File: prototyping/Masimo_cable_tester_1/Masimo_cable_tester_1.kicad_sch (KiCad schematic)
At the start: 27 parts, among them J1 Touchscreen HMI, J12 Barrel_Jack, J16 Debug Connections, J17 Banana Jack, J18 Massimo Connector, J2 Conn_01x28_Socket, J3 Conn_01x28_Socket, J4 SD Card Reader, K2 J104D2C5VDC.15S, U2 LM7805_TO220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

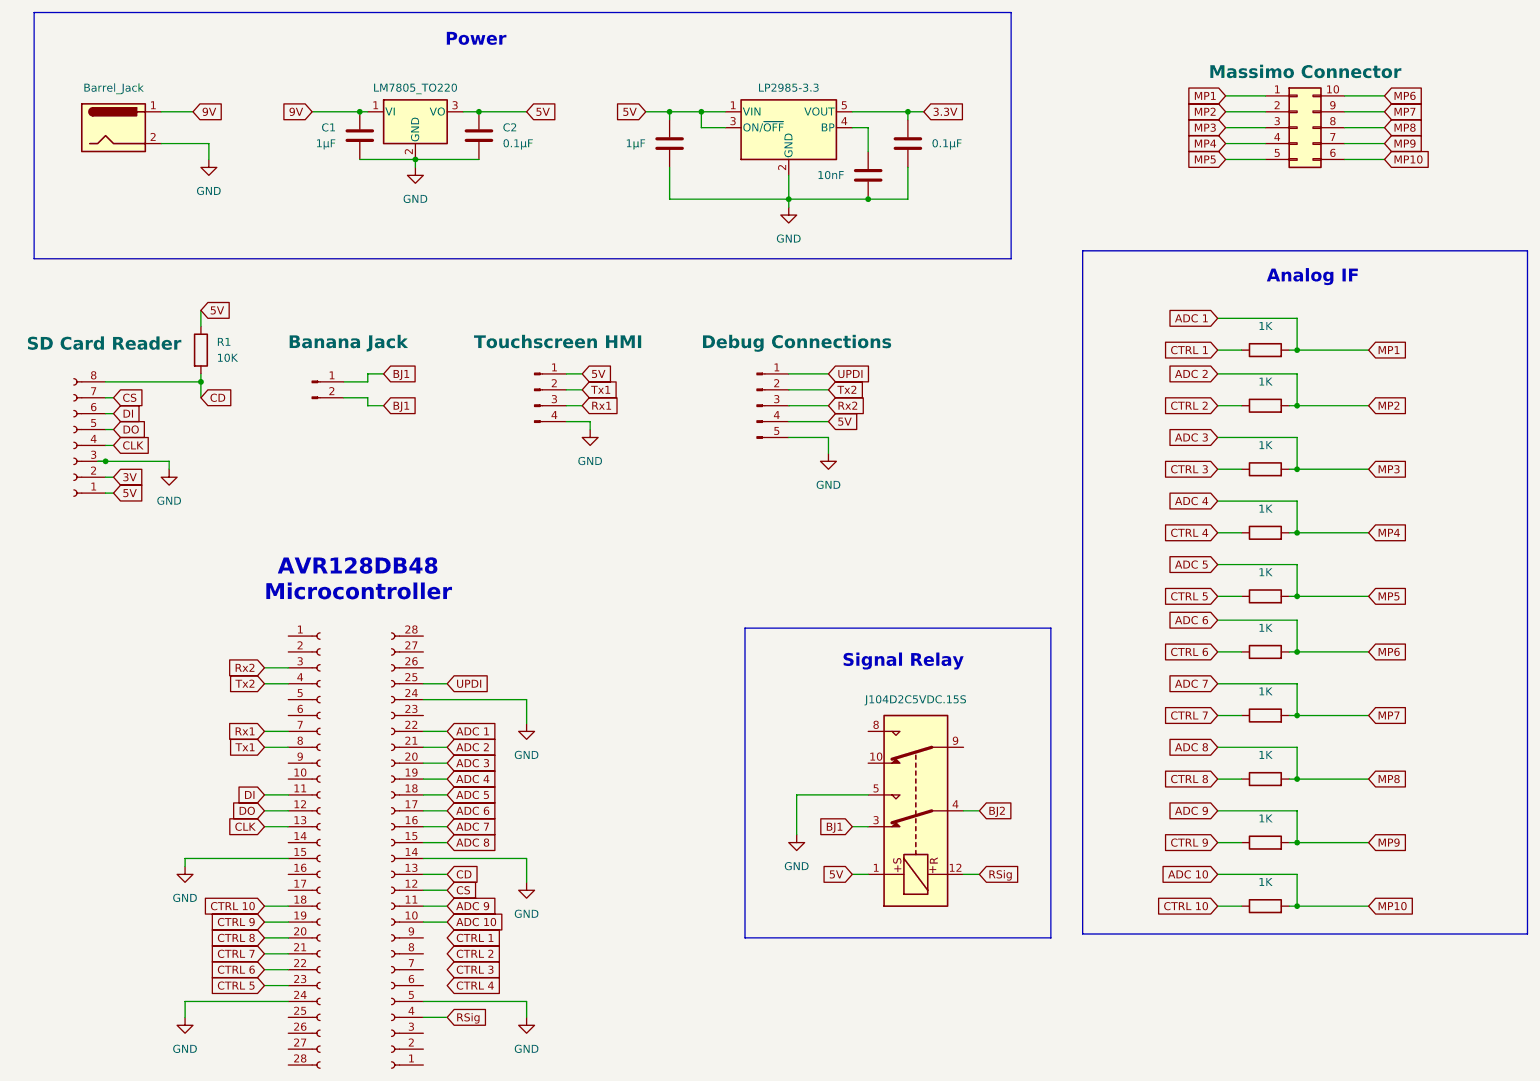
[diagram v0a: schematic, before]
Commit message: Updated the Prototyping PCB schematic
Changed the signal relay symbol and footprint to the correct one. Added a flyback diode to the relay. Added the power required for each resistor. And various general updates to tags and connections.
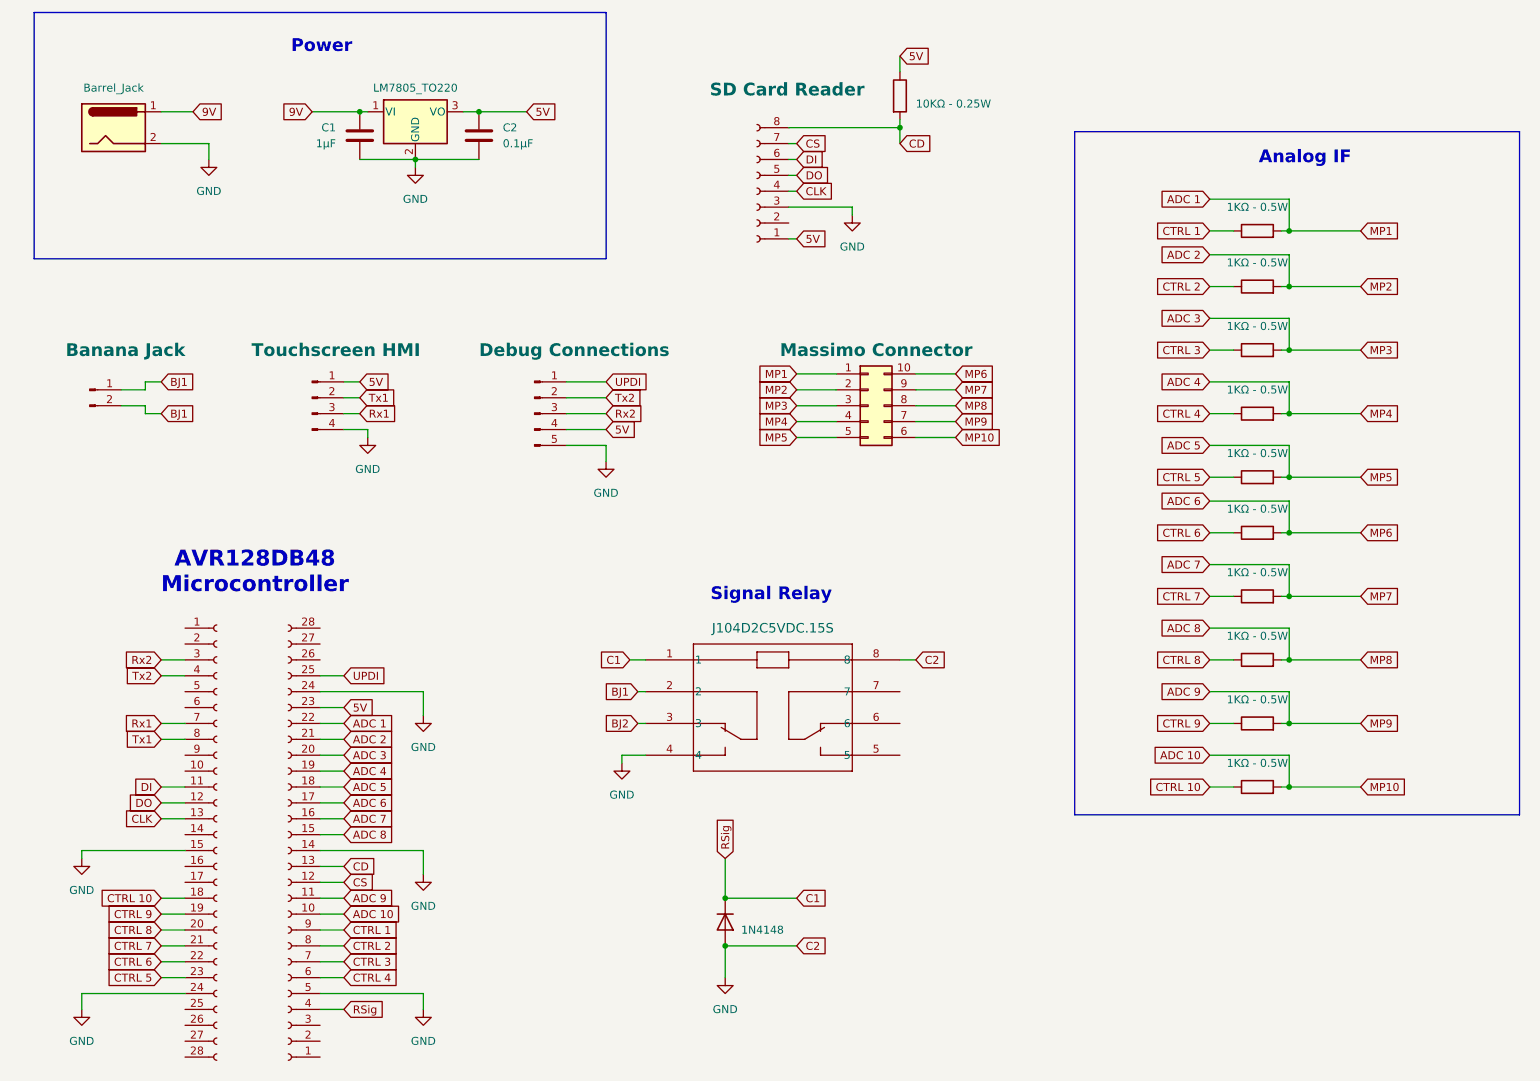
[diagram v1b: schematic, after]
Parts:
- removed C6: 1µF, symbol Device:C
- removed C7: 10nF, symbol Device:C
- removed C8: 0.1µF, symbol Device:C
- removed K2: J104D2C5VDC.15S, Relay_THT:Relay_DPDT_Kemet_EC2, symbol Relay:EC2-5SNU
- removed U3: LP2985-3.3, Package_TO_SOT_SMD:SOT-23-5, symbol Regulator_Linear:LP2985-3.3
- added D1: 1N4148, Diode_THT:D_DO-35_SOD27_P7.62mm_Horizontal, symbol Diode:1N4148
- added U1: J104D2C5VDC.15S, RELAY8_J104D2C5VDC.20S_CRS, symbol 2025-01-29_01-04-30:J104D2C5VDC.20S
- R1: value 10K -> 10KΩ - 0.25W
- R10, R11, R12, R3, R4, R5, R6, R7, R8, R9: value 1K -> 1KΩ - 0.5W
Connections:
- net 5V: now also J3.23 (Pin_23)
- net BJ1: now also U1.2
- net BJ2: now also U1.3
- net CTRL 1: now also J3.9 (Pin_9)
- net CTRL 2: now also J3.8 (Pin_8)
- net CTRL 3: now also J3.7 (Pin_7)
- net CTRL 4: now also J3.6 (Pin_6)
- net GND: now also D1.2 (A), U1.4, U1.8
- net 3V: no longer names the net of J4.2 (Pin_2)
- net RSig renamed C1
- net C1: now also D1.1 (K), U1.1

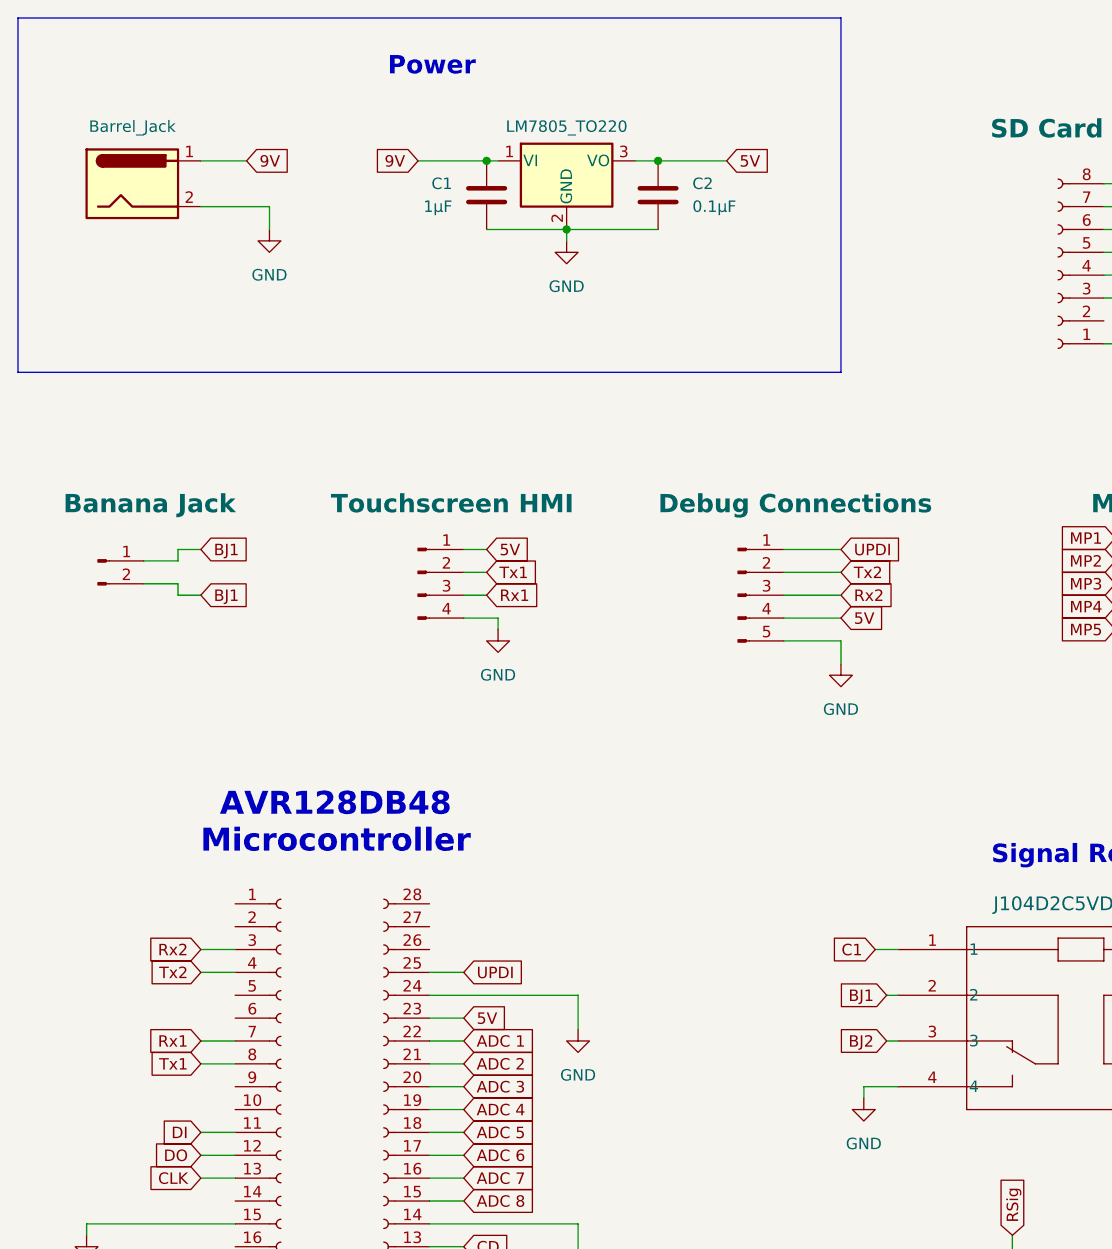
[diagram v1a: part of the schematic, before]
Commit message: Added jumpers
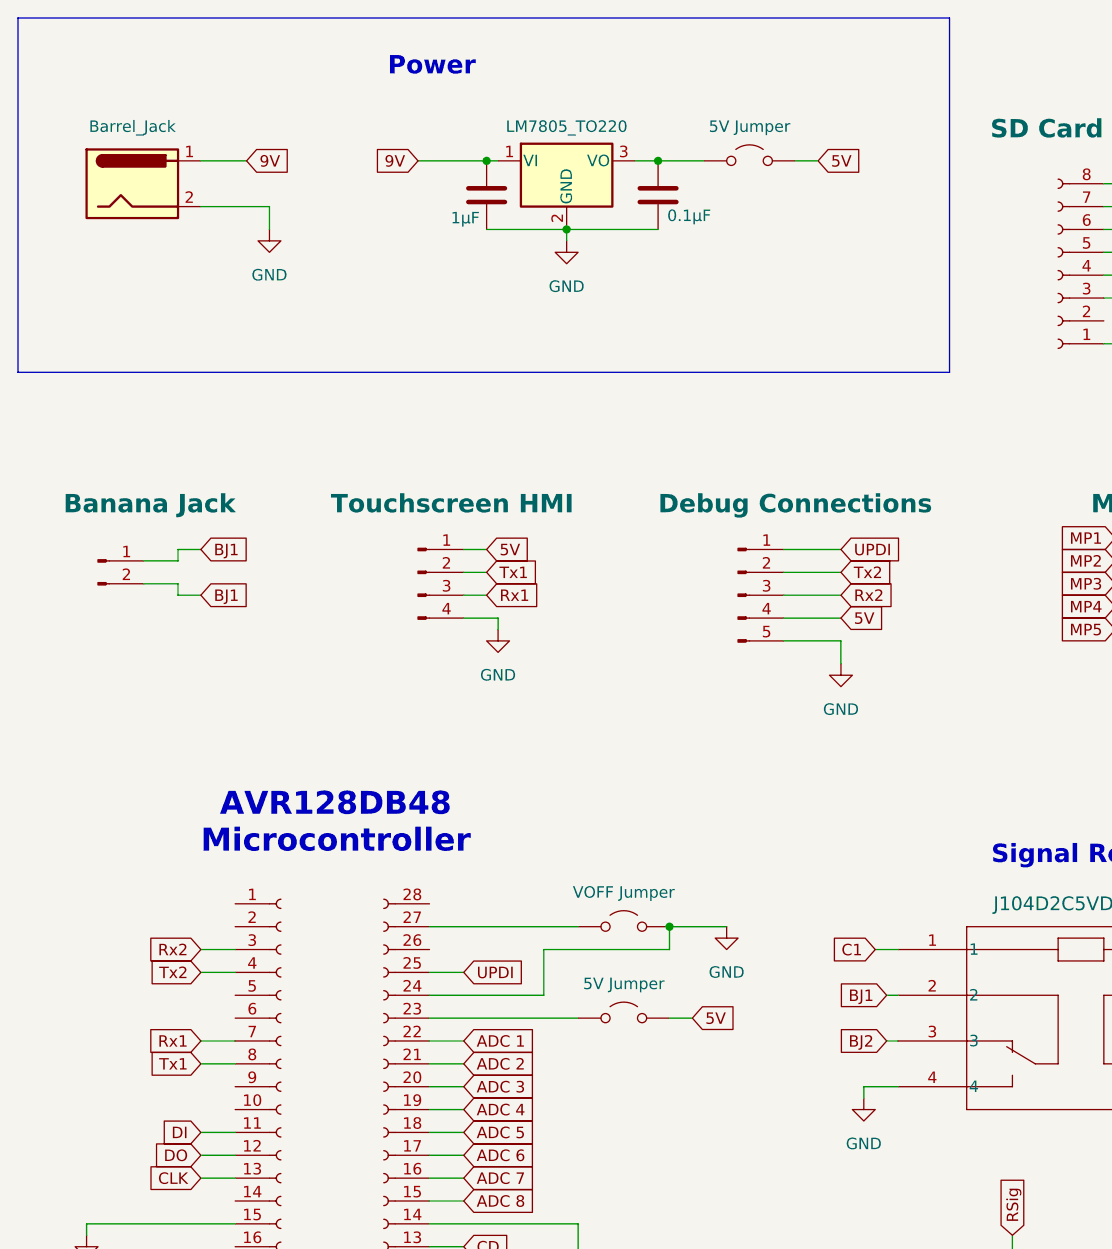
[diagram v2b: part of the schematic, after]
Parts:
- added JP1: VOFF Jumper, symbol Jumper:Jumper_2_Open
- added JP2, JP3: 5V Jumper, symbol Jumper:Jumper_2_Open
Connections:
- net 5V: now also JP2.2 (B), JP3.2 (B); no longer C2.1, J3.23 (Pin_23), U2.3 (VO)
- net GND: now also JP1.2 (B)
- net at J3.27 (Pin_27): now also JP1.1 (A)
- new net: C2.1, JP2.1 (A), U2.3 (VO)
- new net: J3.23 (Pin_23), JP3.1 (A)

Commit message: Attaching footprints to MCU connector and SD card reader
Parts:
- J2, J3: footprint (none) -> Connector_PinHeader_2.54mm:PinHeader_1x28_P2.54mm_Vertical
- J4: footprint (none) -> Connector_PinSocket_1.00mm:PinSocket_1x08_P1.00mm_Vertical
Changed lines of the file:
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@@
 			)
 		)
-		(property "Footprint" ""
+		(property "Footprint" "Connector_PinSocket_1.00mm:PinSocket_1x08_P1.00mm_Vertical"
 			(at 134.62 48.26 0)
 			(effects
@@
 			)
 		)
-		(property "Footprint" ""
+		(property "Footprint" "Connector_PinHeader_2.54mm:PinHeader_1x28_P2.54mm_Vertical"
 			(at 59.69 153.67 0)
 			(effects
@@
 			)
 		)
-		(property "Footprint" ""
+		(property "Footprint" "Connector_PinHeader_2.54mm:PinHeader_1x28_P2.54mm_Vertical"
 			(at 48.26 151.13 0)
 			(effects

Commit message: Prototype schematic updates
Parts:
- removed D1: 1N4148, Diode_THT:D_DO-35_SOD27_P7.62mm_Horizontal, symbol Diode:1N4148
- removed J18: Massimo Connector, symbol Connector_Generic:Conn_02x05_Counter_Clockwise
- removed J4: SD Card Reader, Connector_PinSocket_1.00mm:PinSocket_1x08_P1.00mm_Vertical, symbol Connector:Conn_01x08_Socket
- added D2: 1N4148W-TP, digikey-footprints:SOD-123, symbol dk_Diodes-Rectifiers-Single:1N4148W-TP
- added J5: Conn_01x08, Connector_PinHeader_2.54mm:PinHeader_1x08_P2.54mm_Vertical, symbol Connector_Generic:Conn_01x08
- added J6: SFML-110-02-L-D-A, SFML_110_02_L_D_A:SAMTEC_SFML-110-02-L-D-A, symbol SFML-110-02-L-D-A:SFML-110-02-L-D-A
- added JP4: HMI Power Jumper, symbol Jumper:Jumper_3_Bridged12
- J1: footprint (none) -> Connector_PinHeader_2.54mm:PinHeader_1x04_P2.54mm_Vertical
- J16: footprint (none) -> Connector_PinHeader_2.54mm:PinHeader_1x05_P2.54mm_Vertical
- J17: footprint (none) -> Connector_PinHeader_2.54mm:PinHeader_1x02_P2.54mm_Vertical
- R1: value 10KΩ - 0.25W -> 10kΩ ±0.1% 1/4W
- R10, R11, R12, R3, R4, R5, R6, R7, R8, R9: value 1KΩ - 0.5W -> 1kΩ ±0.1% 0.1W
- U1: footprint RELAY8_J104D2C5VDC.20S_CRS -> footprints:RELAY8_J104D2C5VDC.20S_CRS
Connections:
- net 5V: now also J5.1 (Pin_1), JP4.1 (A); no longer J1.1 (Pin_1)
- net ADC 1: now also J6.01
- net ADC 10: now also J6.10
- net ADC 2: now also J6.03
- net ADC 3: now also J6.05
- net ADC 4: now also J6.07
- net ADC 5: now also J6.09
- net ADC 6: now also J6.02
- net ADC 7: now also J6.04
- net ADC 8: now also J6.06
- net ADC 9: now also J6.08
- net CD: now also J5.8 (Pin_8)
- net CLK: now also J5.4 (Pin_4)
- net CS: now also J5.7 (Pin_7)
- net DI: now also J5.6 (Pin_6)
- net DO: now also J5.5 (Pin_5)
- net GND: now also D2.A, J5.3 (Pin_3)
- net VBUS 5V: now reaches J3.28 (Pin_28)
- net VBUS 5V: now also JP4.3 (B)
- net C1 renamed RSig
- net RSig: now also D2.K
- new net: J1.1 (Pin_1), JP4.2 (C)
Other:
- note added: "20-Pin Connector"
- note added: "MicroSD"
- company: SDSU Senior Design A -> SDSU Senior Design B
- title: Masimo Cable Tester -> Automated multiconductor cable break-short detector

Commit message: Added resistors footprint.
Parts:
- R10, R11, R12, R3, R4, R5, R6, R7, R8, R9: footprint (none) -> RG1608P-102-B-T5:RES_0816_SUS
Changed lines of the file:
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@@
 			)
 		)
-		(property "Footprint" ""
+		(property "Footprint" "RG1608P-102-B-T5:RES_0816_SUS"
 			(at 222.25 71.628 90)
 			(effects
@@
 			)
 		)
-		(property "Footprint" ""
+		(property "Footprint" "RG1608P-102-B-T5:RES_0816_SUS"
 			(at 222.25 91.948 90)
 			(effects
@@
 			)
 		)
-		(property "Footprint" ""
+		(property "Footprint" "RG1608P-102-B-T5:RES_0816_SUS"
 			(at 222.25 131.318 90)
 			(effects
@@
 			)
 		)
-		(property "Footprint" ""
+		(property "Footprint" "RG1608P-102-B-T5:RES_0816_SUS"
 			(at 222.25 102.108 90)
 			(effects
@@
 			)
 		)
-		(property "Footprint" ""
+		(property "Footprint" "RG1608P-102-B-T5:RES_0816_SUS"
 			(at 222.25 141.478 90)
 			(effects
@@
 			)
 		)
-		(property "Footprint" ""
+		(property "Footprint" "RG1608P-102-B-T5:RES_0816_SUS"
 			(at 222.25 110.998 90)
 			(effects
@@
 			)
 		)
-		(property "Footprint" ""
+		(property "Footprint" "RG1608P-102-B-T5:RES_0816_SUS"
 			(at 222.25 62.738 90)
 			(effects
@@
 			)
 		)
-		(property "Footprint" ""
+		(property "Footprint" "RG1608P-102-B-T5:RES_0816_SUS"
 			(at 222.25 121.158 90)
 			(effects
@@
 			)
 		)
-		(property "Footprint" ""
+		(property "Footprint" "RG1608P-102-B-T5:RES_0816_SUS"
 			(at 222.25 151.638 90)
 			(effects
@@
 			)
 		)
-		(property "Footprint" ""
+		(property "Footprint" "RG1608P-102-B-T5:RES_0816_SUS"
 			(at 222.25 81.788 90)
 			(effects

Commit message: Prototype board updates
Added new components with footprints
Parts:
- removed J12: Barrel_Jack, symbol Connector:Barrel_Jack
- removed JP1: VOFF Jumper, symbol Jumper:Jumper_2_Open
- removed JP2, JP3: 5V Jumper, symbol Jumper:Jumper_2_Open
- removed JP4: HMI Power Jumper, symbol Jumper:Jumper_3_Bridged12
- added J10: 5V Jumper, symbol Connector:Conn_01x02_Pin
- added J4: Barrel Jack 9V, 54_00129:TENSILITY_54-00129, symbol 54-00129:54-00129
- added J7: Conn_01x03_Pin, Connector_PinHeader_2.54mm:PinHeader_1x03_P2.54mm_Vertical, symbol Connector:Conn_01x03_Pin
- added J8: Jumper Pins 5V, symbol Connector:Conn_01x02_Pin
- added J9: VOFF Jumper, symbol Connector:Conn_01x02_Pin
- R1: footprint (none) -> footprints:RC0402N_PAN
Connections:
- net 5V: now also J10.2 (Pin_2), J7.3 (Pin_3), J8.1 (Pin_1)
- net 9V: now also J4.A
- net GND: now also J4.C, J9.1 (Pin_1)
- net VBUS 5V: now also J7.1 (Pin_1)
- net at C2.1, U2.3 (VO): now also J8.2 (Pin_2)
- net at J1.1 (Pin_1): now also J7.2 (Pin_2)
- net at J3.27 (Pin_27): now also J9.2 (Pin_2)
- net at J3.23 (Pin_23): now also J10.1 (Pin_1)

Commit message: Added capacitor footprints.
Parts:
- C1: footprint (none) -> CL10B105KP8NNNC:CAP_CL10_SAM
- C2: footprint (none) -> CL05B104KP5NNNC:CAP_CL05_SAM
- R1: footprint footprints:RC0402N_PAN -> ERJ_2RKF1002X:RC0402N_PAN
- U1: footprint footprints:RELAY8_J104D2C5VDC.20S_CRS -> J104D2C5VDC.20S:RELAY8_J104D2C5VDC.20S_CRS
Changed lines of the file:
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@@
 			)
 		)
-		(property "Footprint" ""
+		(property "Footprint" "CL05B104KP5NNNC:CAP_CL05_SAM"
 			(at 91.1352 48.26 0)
 			(effects
@@
 			)
 		)
-		(property "Footprint" "footprints:RC0402N_PAN"
+		(property "Footprint" "ERJ_2RKF1002X:RC0402N_PAN"
 			(at 160.782 31.75 90)
 			(effects
@@
 			)
 		)
-		(property "Footprint" ""
+		(property "Footprint" "CL10B105KP8NNNC:CAP_CL10_SAM"
 			(at 70.1548 48.26 0)
 			(effects
@@
 			)
 		)
-		(property "Footprint" "footprints:RELAY8_J104D2C5VDC.20S_CRS"
+		(property "Footprint" "J104D2C5VDC.20S:RELAY8_J104D2C5VDC.20S_CRS"
 			(at 125.73 143.51 0)
 			(effects
